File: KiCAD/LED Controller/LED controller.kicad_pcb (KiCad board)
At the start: 2 copper layers, 100 x 100 mm, 42 parts, among them J1 Barrel_Jack_Switch, J2 4x RJ45, J5 8P8C_Shielded, SW1 ELUMOASAQ2C22, SW2 ELUMOASAQ2C22, SW3 ELUMOASAQ2C22, U1 SN75374D, U2 SN75374D, U3 SN75374D, U4 Teensy4.1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

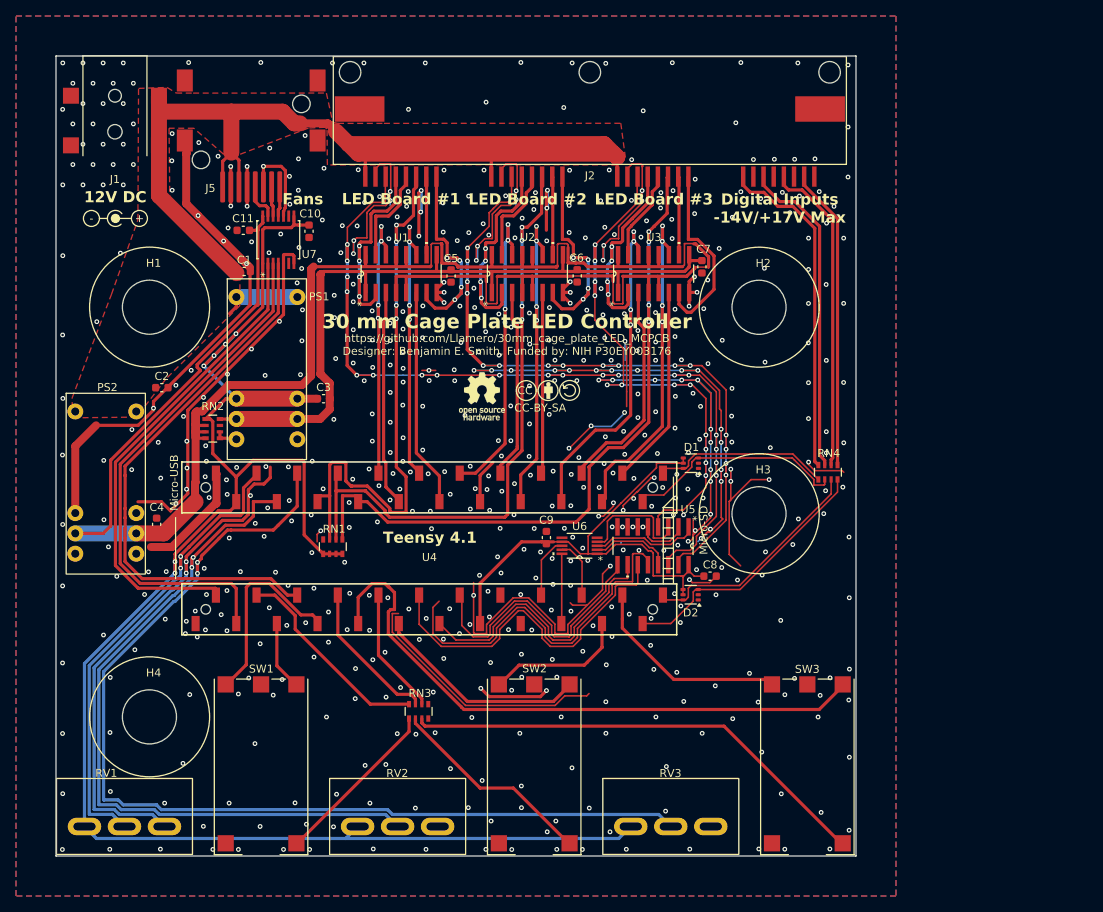
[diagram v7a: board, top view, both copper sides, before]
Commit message: I2C and external LED connector added - Pass DRC
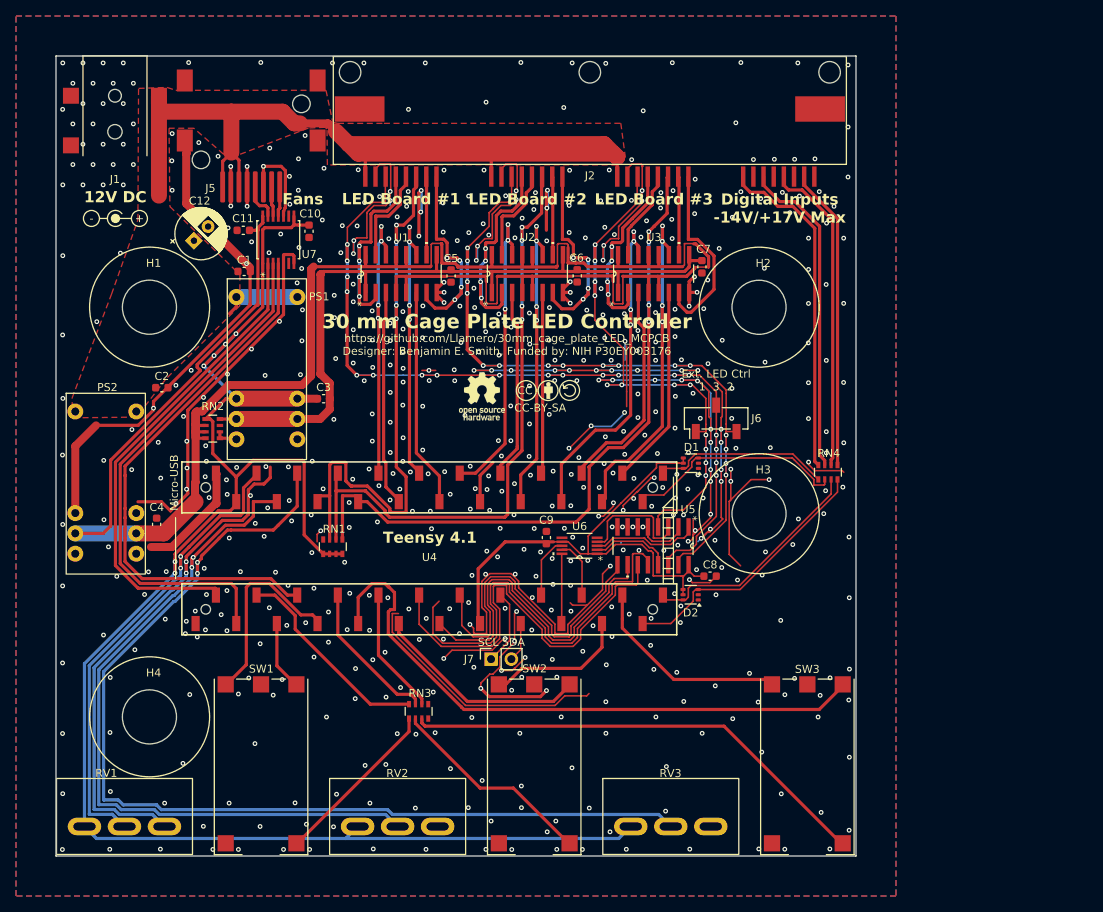
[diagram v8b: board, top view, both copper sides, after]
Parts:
- added C12: 220µF, Capacitor_THT:CP_Radial_D6.3mm_P2.50mm, F.Cu at (17.2, 23.1)
- added J6: Conn_01x03_Socket, Connector_PinSocket_2.54mm:PinSocket_1x03_P2.54mm_Vertical_SMD_Pin1Left, F.Cu at (82.5, 45.3)
- added J7: Conn_01x02_Socket, Connector_PinSocket_2.54mm:PinSocket_1x02_P2.54mm_Vertical, F.Cu at (54.4, 75.4)
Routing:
- net GND: track 620.5 -> 646.7 mm, vias 617 -> 620
- net /12V: track 154.0 -> 140.3 mm
- net /SCL: track 0.00 -> 9.38 mm
- net /LED_PWM1: track 44.0 -> 51.5 mm
- net /LED_PWM2: track 36.4 -> 43.6 mm
- net /LED_PWM3: track 34.7 -> 41.8 mm
- net /SDA: track 0.00 -> 4.93 mm
- net /3v3: track 276.0 -> 277.4 mm
- net /Ctrl2: track 101.4 -> 102.7 mm
- net /Ctrl3: track 73.9 -> 75.2 mm
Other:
- board text added: "Ext. LED Ctrl 1 3 2"
- board text added: "SCL SDA"
